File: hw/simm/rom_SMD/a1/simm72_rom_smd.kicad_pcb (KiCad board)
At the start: 4 copper layers, 108 x 19.1 mm, 7 parts, among them IC1 SN74LVC2G08DCUR, IC2 SST39LFx01, IC3 SST39LFx01, J1 SIMM72

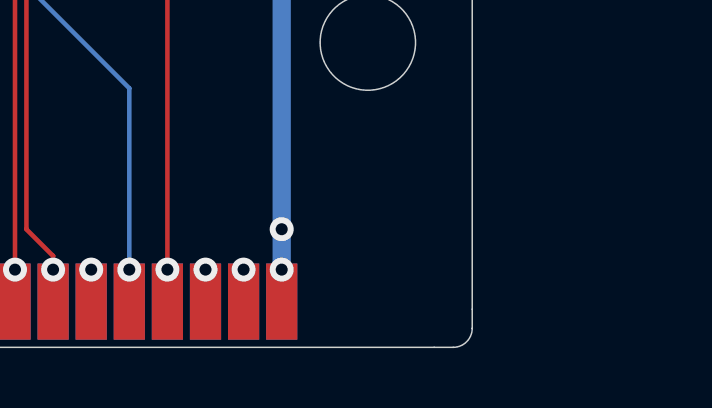
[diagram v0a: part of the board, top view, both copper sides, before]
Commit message: update SMD-ROM rev.A1 with gerbers
Has not been built nor tested.
Should be compatible with existing rom chips, and can in theory support additional models with byte/word select input (assuming software for flashing is updated to support the model if required)
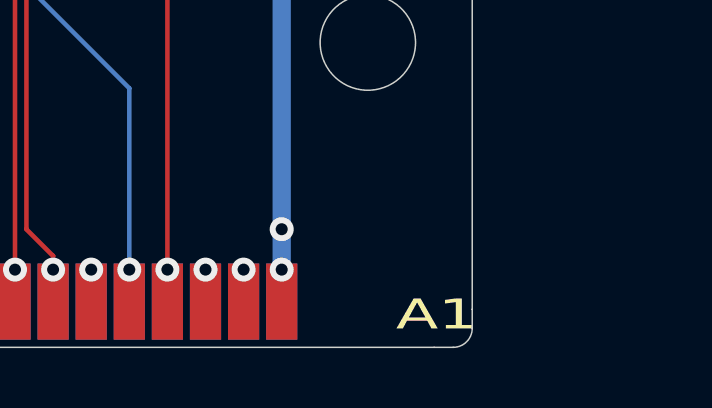
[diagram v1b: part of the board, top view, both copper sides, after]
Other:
- board text added: "/BYTE"
- board text added: "A1"
